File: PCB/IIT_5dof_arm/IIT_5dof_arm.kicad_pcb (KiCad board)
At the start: 2 copper layers, 100 x 100 mm, 59 parts, among them J1 Screw_Terminal_01x02, J2 Conn_01x06, J3 Conn_01x06, J4 Conn_01x06, J5 Conn_01x06, J6 Conn_01x06, J7 Conn_01x06, J9 DE9_Receptacle_MountingHoles, SW1 SW_MAIN, SW15 SW_MOT, U5 XL8574T, U6 MAX3232, U9 4504

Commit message: Eliminate GNDPWR
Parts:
- C10, C11, C12: value 0.1uF -> 10uF
- D5: value SMAJ12A -> SMAJ5.0A
- moved C12 6.08 mm to (136.1, 86.4), turned to 90 degrees
- moved C10 5.80 mm to (127.4, 88.8), turned to -90 degrees
- moved C11 2.62 mm to (64.5, 57.5), turned to 90 degrees
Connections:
- C10 pad 2: GNDPWR -> GND
- C11 pad 2: GNDPWR -> GND
- C12 pad 2: GNDPWR -> GND
- C14 pad 2: GNDPWR -> GND
- D19 pad 2: GNDPWR -> GND
- J1 pad 1: GNDPWR -> GND
- PS1 pad 2: GNDPWR -> GND
- R36 pad 2: GNDPWR -> GND
- SW15 pad 3: GNDPWR -> GND
- U1 pad 4: GNDPWR -> GND
- U2 pad 4: GNDPWR -> GND
- U3 pad 4: GNDPWR -> GND
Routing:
- net GNDPWR: track 204.8 -> 0.00 mm
- net GND: track 2.54 -> 14.0 mm, vias 21 -> 23
- net /mot1_A: track 67.9 -> 69.5 mm
- net /mot1_B: track 65.9 -> 67.2 mm

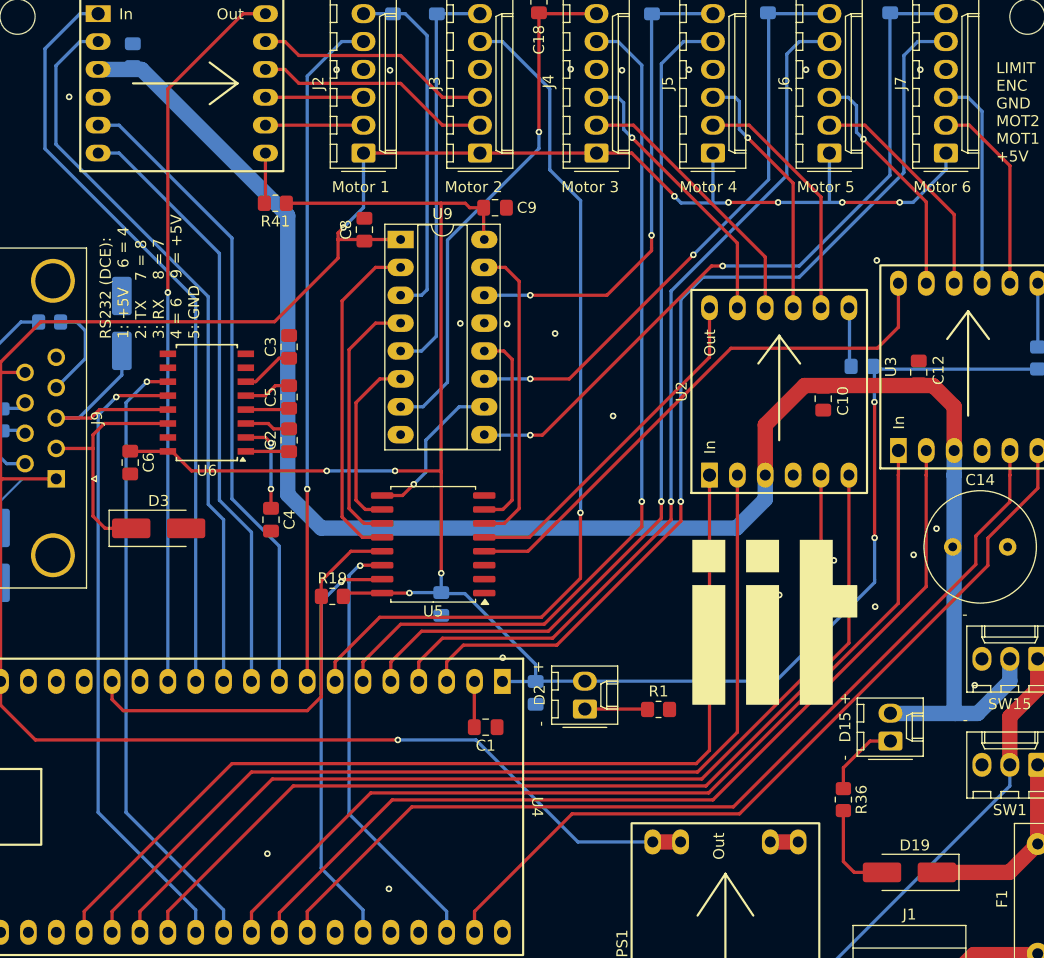
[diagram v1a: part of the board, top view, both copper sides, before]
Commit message: Remove unnecessary vias
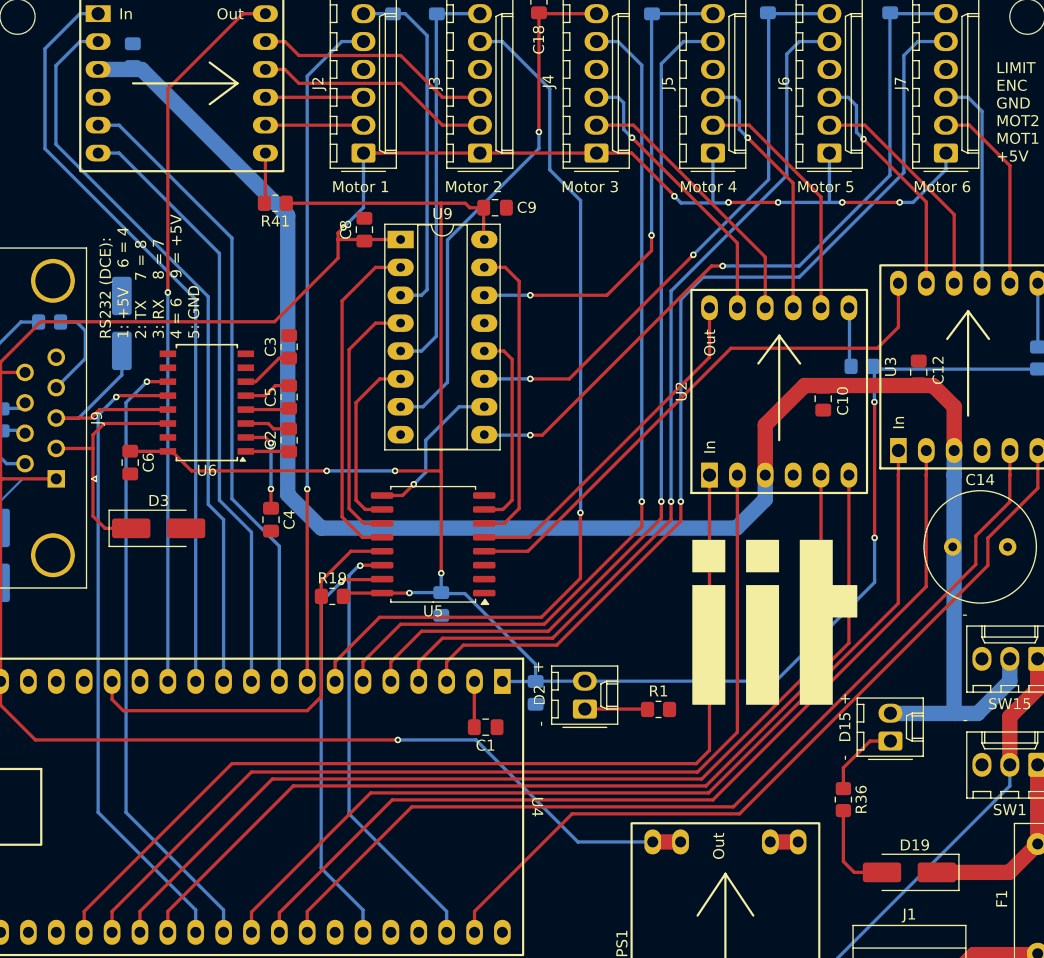
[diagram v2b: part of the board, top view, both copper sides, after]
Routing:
- net GND: vias 23 -> 0
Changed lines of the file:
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@@
 		(tags "capacitor handsolder")
 		(property "Reference" "C12"
-			(at 0.2 1.8 270)
+			(at 0.2 1.8 -90)
 			(layer "F.SilkS")
 			(effects
@@
 		)
 		(property "Value" "10uF"
-			(at 0 1.68 270)
+			(at 0 1.68 -90)
 			(layer "F.Fab")
 			(effects
@@
 		)
 		(fp_text user "${REFERENCE}"
-			(at 0 0 270)
+			(at 0 0 -90)
 			(layer "F.Fab")
 			(effects
@@
 		(tags "capacitor handsolder")
 		(property "Reference" "C11"
-			(at 0.4 1.9 270)
+			(at 0.4 1.9 -90)
 			(layer "B.SilkS")
 			(effects
@@
 		)
 		(property "Value" "10uF"
-			(at 0 -1.68 270)
+			(at 0 -1.68 -90)
 			(layer "B.Fab")
 			(effects
@@
 		)
 		(fp_text user "${REFERENCE}"
-			(at 0 0 270)
+			(at 0 0 -90)
 			(layer "B.Fab")
 			(effects
@@
 		(net 1)
 	)
-	(via
-		(at 125.8316 58.8264)
-		(size 0.6)
-		(drill 0.3)
-		(layers "F.Cu" "B.Cu")
-		(free yes)
-		(net 1)
-	)
-	(via
-		(at 123.3932 106.68)
-		(size 0.6)
-		(drill 0.3)
-		(layers "F.Cu" "B.Cu")
-		(free yes)
-		(net 1)
-	)
-	(via
-		(at 135.636 103.0224)
-		(size 0.6)
-		(drill 0.3)
-		(layers "F.Cu" "B.Cu")
-		(free yes)
-		(net 1)
-	)
-	(via
-		(at 118.11 110.2868)
-		(size 0.6)
-		(drill 0.3)
-		(layers "F.Cu" "B.Cu")
-		(free yes)
-		(net 1)
-	)
-	(via
-		(at 104.394 58.7756)
-		(size 0.6)
-		(drill 0.3)
-		(layers "F.Cu" "B.Cu")
-		(free yes)
-		(net 1)
-	)
-	(via
-		(at 83.058 58.8264)
-		(size 0.6)
-		(drill 0.3)
-		(layers "F.Cu" "B.Cu")
-		(free yes)
-		(net 1)
-	)
-	(via
-		(at 132.1308 107.7468)
-		(size 0.6)
-		(drill 0.3)
-		(layers "F.Cu" "B.Cu")
-		(free yes)
-		(net 1)
-	)
-	(via
-		(at 115.1636 58.8264)
-		(size 0.6)
-		(drill 0.3)
-		(layers "F.Cu" "B.Cu")
-		(free yes)
-		(net 1)
-	)
-	(via
-		(at 98.2 112.4)
-		(size 0.6)
-		(drill 0.3)
-		(layers "F.Cu" "B.Cu")
-		(free yes)
-		(net 1)
-	)
-	(via
-		(at 137.7188 100.6348)
-		(size 0.6)
-		(drill 0.3)
-		(layers "F.Cu" "B.Cu")
-		(free yes)
-		(net 1)
-	)
-	(via
-		(at 98.6028 81.9912)
-		(size 0.6)
-		(drill 0.3)
-		(layers "F.Cu" "B.Cu")
-		(free yes)
-		(net 1)
-	)
-	(via
-		(at 109.0676 58.8772)
-		(size 0.6)
-		(drill 0.3)
-		(layers "F.Cu" "B.Cu")
-		(free yes)
-		(net 1)
-	)
-	(via
-		(at 141.2 114.9)
-		(size 0.6)
-		(drill 0.3)
-		(layers "F.Cu" "B.Cu")
-		(free yes)
-		(net 1)
-	)
-	(via
-		(at 76.7588 130.2512)
-		(size 0.6)
-		(drill 0.3)
-		(layers "F.Cu" "B.Cu")
-		(free yes)
-		(net 1)
-	)
-	(via
-		(at 128.3716 103.5304)
-		(size 0.6)
-		(drill 0.3)
-		(layers "F.Cu" "B.Cu")
-		(free yes)
-		(net 1)
-	)
-	(via
-		(at 108.2548 90.3732)
-		(size 0.6)
-		(drill 0.3)
-		(layers "F.Cu" "B.Cu")
-		(free yes)
-		(net 1)
-	)
-	(via
-		(at 102.9716 82.8548)
-		(size 0.6)
-		(drill 0.3)
-		(layers "F.Cu" "B.Cu")
-		(free yes)
-		(net 1)
-	)
-	(via
-		(at 87.9348 58.8772)
-		(size 0.6)
-		(drill 0.3)
-		(layers "F.Cu" "B.Cu")
-		(free yes)
-		(net 1)
-	)
-	(via
-		(at 132.2832 76.2)
-		(size 0.6)
-		(drill 0.3)
-		(layers "F.Cu" "B.Cu")
-		(free yes)
-		(net 1)
-	)
-	(via
-		(at 136.2456 58.8264)
-		(size 0.6)
-		(drill 0.3)
-		(layers "F.Cu" "B.Cu")
-		(free yes)
-		(net 1)
-	)
-	(via
-		(at 94.3356 81.9404)
-		(size 0.6)
-		(drill 0.3)
-		(layers "F.Cu" "B.Cu")
-		(free yes)
-		(net 1)
-	)
-	(via
-		(at 87.8332 133.4516)
-		(size 0.6)
-		(drill 0.3)
-		(layers "F.Cu" "B.Cu")
-		(free yes)
-		(net 1)
-	)
-	(via
-		(at 58.7 61.3)
-		(size 0.6)
-		(drill 0.3)
-		(layers "F.Cu" "B.Cu")
-		(free yes)
-		(net 1)
-	)

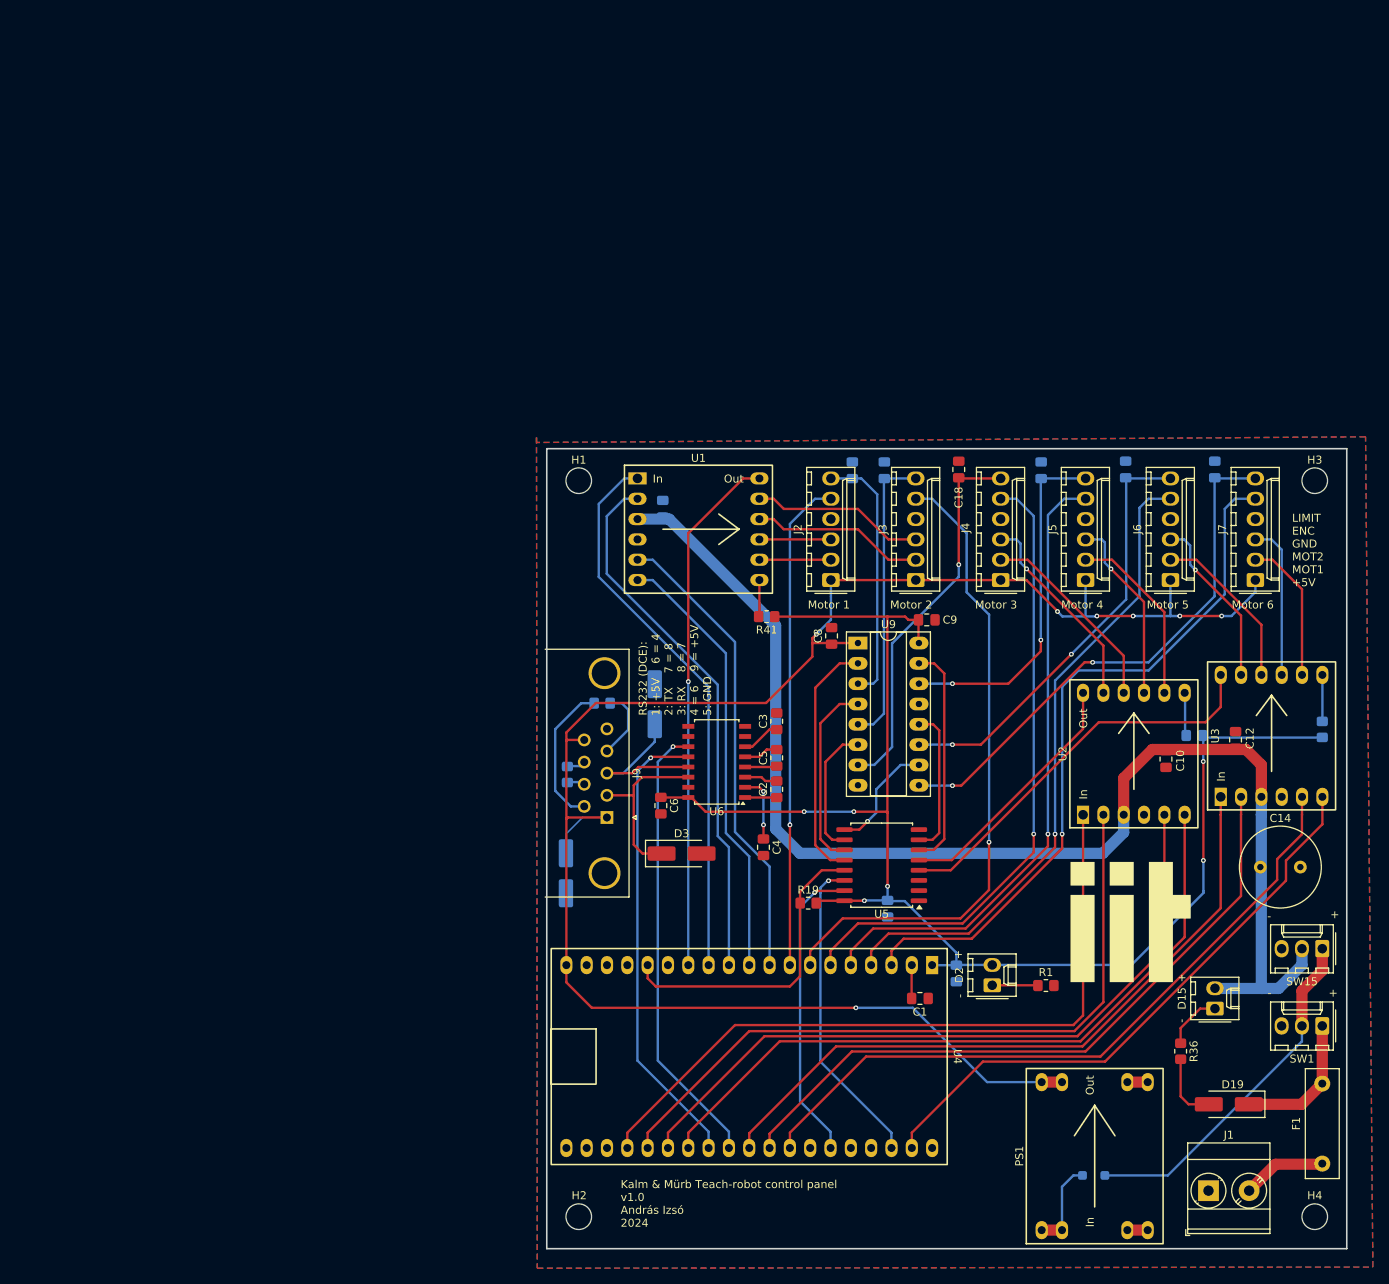
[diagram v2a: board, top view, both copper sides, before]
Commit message: Update schematic with new functionalities
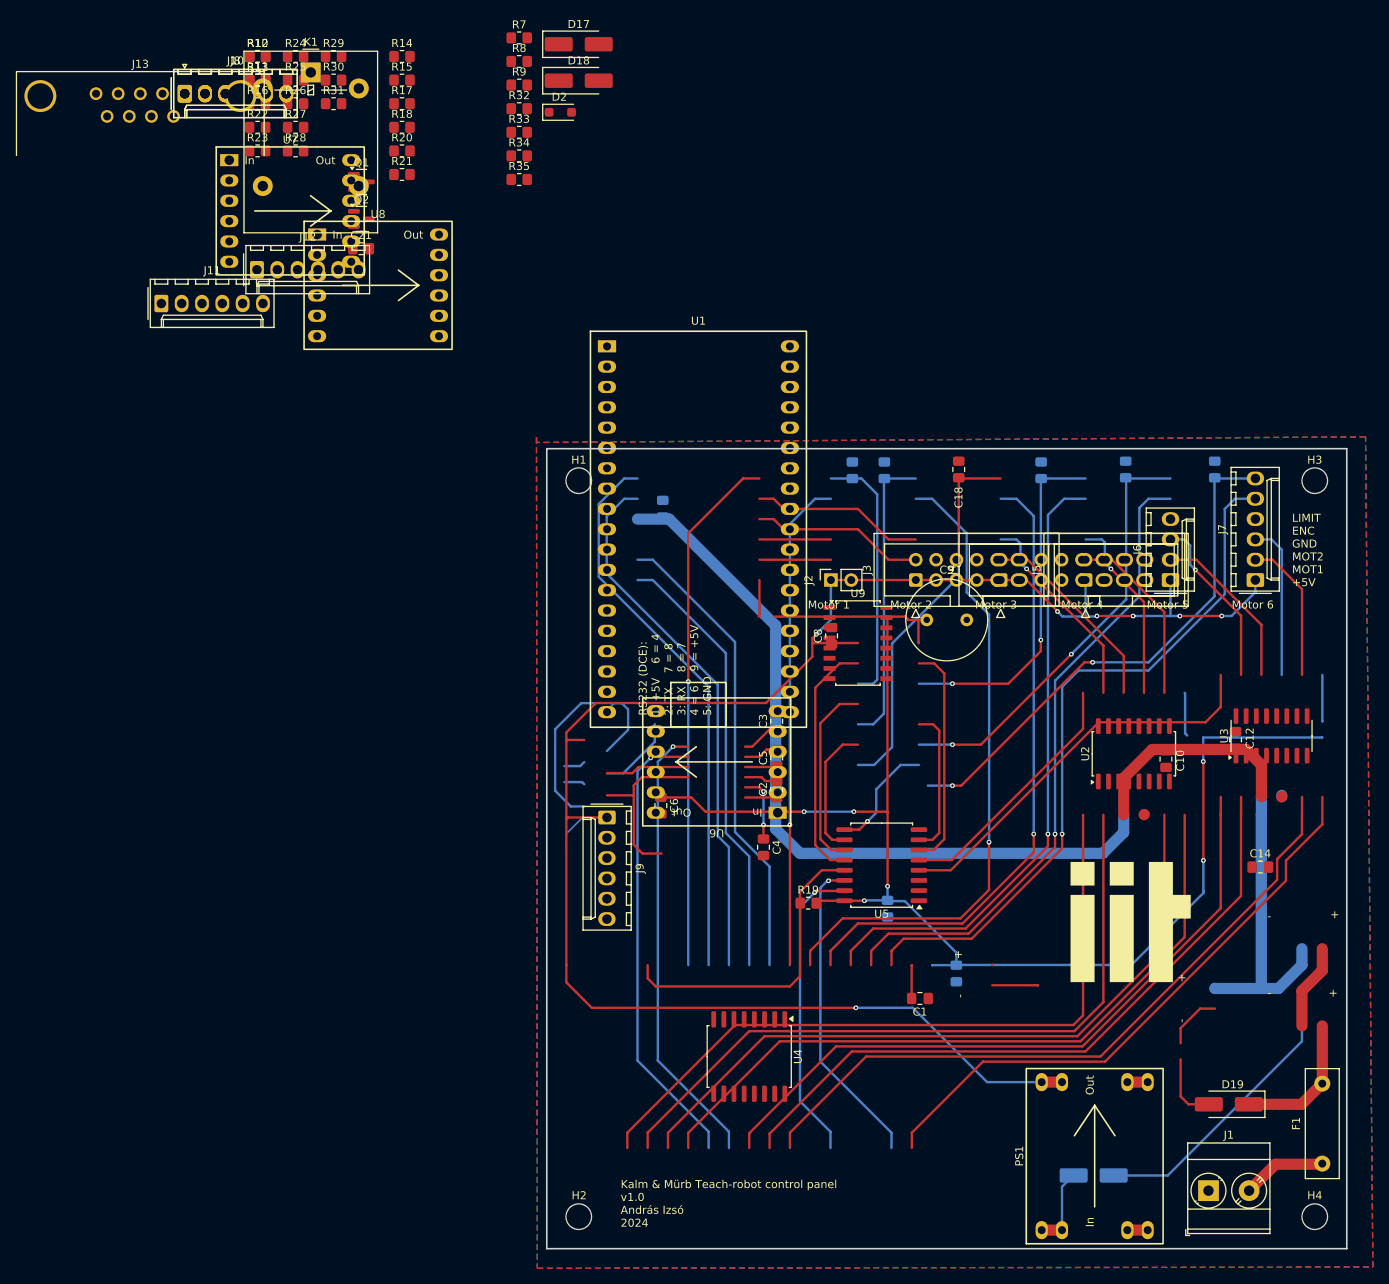
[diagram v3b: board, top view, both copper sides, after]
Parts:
- removed D15: LED, Connector_Molex:Molex_KK-254_AE-6410-02A_1x02_P2.54mm_Vertical
- removed D3, D4: SMAJ12A, Diode_SMD:D_SMA_Handsoldering
- removed D5: SMAJ5.0A, Diode_SMD:D_SMA_Handsoldering
- removed R1: 220, Resistor_SMD:R_0805_2012Metric_Pad1.20x1.40mm_HandSolder
- removed R2, R3: 1k, Resistor_SMD:R_0805_2012Metric_Pad1.20x1.40mm_HandSolder
- removed R36: 590, Resistor_SMD:R_0805_2012Metric_Pad1.20x1.40mm_HandSolder
- removed R41, R42, R43: 10k, Resistor_SMD:R_0805_2012Metric_Pad1.20x1.40mm_HandSolder
- removed SW1: SW_MAIN, Connector_Molex:Molex_KK-254_AE-6410-03A_1x03_P2.54mm_Vertical
- removed SW15: SW_MOT, Connector_Molex:Molex_KK-254_AE-6410-03A_1x03_P2.54mm_Vertical
- added C21: 0.1uF, Capacitor_SMD:C_0805_2012Metric_Pad1.18x1.45mm_HandSolder, F.Cu at (26.8, 25.0)
- added D17: SMAJ12A, Diode_SMD:D_SMA_Handsoldering, F.Cu at (54.0, -0.55)
- added D18: SMAJ12A, Diode_SMD:D_SMA_Handsoldering, F.Cu at (54.0, 4.00)
- added J10, J8: Conn_01x06, Connector_Molex:Molex_KK-254_AE-6410-06A_1x06_P2.54mm_Vertical, F.Cu at (4.74, 5.62)
- added J11: Conn_01x06, Connector_Molex:Molex_KK-254_AE-6410-06A_1x06_P2.54mm_Vertical, F.Cu at (1.82, 31.9)
- added J12: Conn_01x06, Connector_Molex:Molex_KK-254_AE-6410-06A_1x06_P2.54mm_Vertical, F.Cu at (13.8, 27.6)
- added J13: DE9_Receptacle_MountingHoles, Connector_Dsub:DSUB-9_Female_Horizontal_P2.77x2.84mm_EdgePinOffset4.94mm_Housed_MountingHolesOffset7.48mm, F.Cu at (4.74, 5.62)
- added K1: G5LE-1, Relay_THT:Relay_SPDT_Omron-G5LE-1, F.Cu at (20.5, 2.97)
- added Q1: 2N7002, Package_TO_SOT_SMD:SOT-23, F.Cu at (26.8, 16.6)
- added Q2: 2N7002, Package_TO_SOT_SMD:SOT-23, F.Cu at (26.8, 21.3)
- added R10, R12: 1k, Resistor_SMD:R_0805_2012Metric_Pad1.20x1.40mm_HandSolder, F.Cu at (13.9, 0.97)
- added R11: 1k, Resistor_SMD:R_0805_2012Metric_Pad1.20x1.40mm_HandSolder, F.Cu at (13.9, 3.92)
- added R13: 10k, Resistor_SMD:R_0805_2012Metric_Pad1.20x1.40mm_HandSolder, F.Cu at (13.9, 3.92)
- added R14: 10k, Resistor_SMD:R_0805_2012Metric_Pad1.20x1.40mm_HandSolder, F.Cu at (31.9, 0.97)
- added R15: 1k, Resistor_SMD:R_0805_2012Metric_Pad1.20x1.40mm_HandSolder, F.Cu at (31.9, 3.92)
- added R16: 10k, Resistor_SMD:R_0805_2012Metric_Pad1.20x1.40mm_HandSolder, F.Cu at (13.9, 6.88)
- added R17: 1k, Resistor_SMD:R_0805_2012Metric_Pad1.20x1.40mm_HandSolder, F.Cu at (31.9, 6.88)
- added R18: 3k, Resistor_SMD:R_0805_2012Metric_Pad1.20x1.40mm_HandSolder, F.Cu at (31.9, 9.82)
- added R20: 3k, Resistor_SMD:R_0805_2012Metric_Pad1.20x1.40mm_HandSolder, F.Cu at (31.9, 12.8)
- added R21: 3k, Resistor_SMD:R_0805_2012Metric_Pad1.20x1.40mm_HandSolder, F.Cu at (31.9, 15.7)
- added R22: 3k, Resistor_SMD:R_0805_2012Metric_Pad1.20x1.40mm_HandSolder, F.Cu at (13.9, 9.82)
- added R23: 3k, Resistor_SMD:R_0805_2012Metric_Pad1.20x1.40mm_HandSolder, F.Cu at (13.9, 12.8)
- added R24: 10k, Resistor_SMD:R_0805_2012Metric_Pad1.20x1.40mm_HandSolder, F.Cu at (18.6, 0.97)
- added R25: 10k, Resistor_SMD:R_0805_2012Metric_Pad1.20x1.40mm_HandSolder, F.Cu at (18.6, 3.92)
- added R26: 10k, Resistor_SMD:R_0805_2012Metric_Pad1.20x1.40mm_HandSolder, F.Cu at (18.6, 6.88)
- added R27: 10k, Resistor_SMD:R_0805_2012Metric_Pad1.20x1.40mm_HandSolder, F.Cu at (18.6, 9.82)
- added R28: 4k7, Resistor_SMD:R_0805_2012Metric_Pad1.20x1.40mm_HandSolder, F.Cu at (18.6, 12.8)
- added R29: 10k, Resistor_SMD:R_0805_2012Metric_Pad1.20x1.40mm_HandSolder, F.Cu at (23.4, 0.97)
- added R30: 4k7, Resistor_SMD:R_0805_2012Metric_Pad1.20x1.40mm_HandSolder, F.Cu at (23.4, 3.92)
- added R31: 10k, Resistor_SMD:R_0805_2012Metric_Pad1.20x1.40mm_HandSolder, F.Cu at (23.4, 6.88)
- added R32: 1k, Resistor_SMD:R_0805_2012Metric_Pad1.20x1.40mm_HandSolder, F.Cu at (46.6, 7.50)
- added R33: 10k, Resistor_SMD:R_0805_2012Metric_Pad1.20x1.40mm_HandSolder, F.Cu at (46.6, 10.4)
- added R34: 1k, Resistor_SMD:R_0805_2012Metric_Pad1.20x1.40mm_HandSolder, F.Cu at (46.6, 13.4)
- added R35: 2k, Resistor_SMD:R_0805_2012Metric_Pad1.20x1.40mm_HandSolder, F.Cu at (46.6, 16.4)
- added R7: 220, Resistor_SMD:R_0805_2012Metric_Pad1.20x1.40mm_HandSolder, F.Cu at (46.6, -1.35)
- added R8: 100k, Resistor_SMD:R_0805_2012Metric_Pad1.20x1.40mm_HandSolder, F.Cu at (46.6, 1.60)
- added R9: 10k, Resistor_SMD:R_0805_2012Metric_Pad1.20x1.40mm_HandSolder, F.Cu at (46.6, 4.55)
- added U7: ~, IIT_5dof_arm:DRV8833-M, F.Cu at (17.9, 20.3)
- added U8: ~, IIT_5dof_arm:DRV8833-M, F.Cu at (28.9, 29.6)
- C1, C17, C18, C19, C20: value 10nF -> 0.1uF
- C10, C11: value 10uF -> 0.1uF
- C14: value 1000uF -> 0.1uF; footprint Capacitor_THT:C_Radial_D10.0mm_H16.0mm_P5.00mm -> Capacitor_SMD:C_0805_2012Metric_Pad1.18x1.45mm_HandSolder
- C15, C16: value 10nF -> 10uF
- C2, C3, C4, C5, C6, C7, C8: value 0.1uF -> 10nF
- C9: value 0.1uF -> 1000uF; footprint Capacitor_SMD:C_0805_2012Metric_Pad1.18x1.45mm_HandSolder -> Capacitor_THT:C_Radial_D10.0mm_H16.0mm_P5.00mm
- D1: value D_Schottky -> SMAJ12A; footprint Diode_SMD:D_SOD-123F -> Diode_SMD:D_SMA_Handsoldering
- D19: value SMAJ12A -> SMAJ5.0A
- D2: value LED -> D_Schottky; footprint Connector_Molex:Molex_KK-254_AE-6410-02A_1x02_P2.54mm_Vertical -> Diode_SMD:D_SOD-123F
- J2: value Conn_01x06 -> Conn_01x02; footprint Connector_Molex:Molex_KK-254_AE-6410-06A_1x06_P2.54mm_Vertical -> Connector_PinSocket_2.54mm:PinSocket_1x02_P2.54mm_Vertical
- J3: value Conn_01x06 -> Conn_02x06_Odd_Even; footprint Connector_Molex:Molex_KK-254_AE-6410-06A_1x06_P2.54mm_Vertical -> Connector_IDC:IDC-Header_2x06_P2.54mm_Vertical
- J4: value Conn_01x06 -> Conn_02x08_Odd_Even; footprint Connector_Molex:Molex_KK-254_AE-6410-06A_1x06_P2.54mm_Vertical -> Connector_IDC:IDC-Header_2x08_P2.54mm_Vertical
- J5: value Conn_01x06 -> Conn_02x04_Odd_Even; footprint Connector_Molex:Molex_KK-254_AE-6410-06A_1x06_P2.54mm_Vertical -> Connector_IDC:IDC-Header_2x04_P2.54mm_Vertical
- J6: value Conn_01x06 -> Conn_01x04; footprint Connector_Molex:Molex_KK-254_AE-6410-06A_1x06_P2.54mm_Vertical -> Connector_Molex:Molex_KK-254_AE-6410-04A_1x04_P2.54mm_Vertical
- J9: value DE9_Receptacle_MountingHoles -> Conn_01x06; footprint Connector_Dsub:DSUB-9_Female_Horizontal_P2.77x2.84mm_EdgePinOffset4.94mm_Housed_MountingHolesOffset7.48mm -> Connector_Molex:Molex_KK-254_AE-6410-06A_1x06_P2.54mm_Vertical
- R19: value 10k -> 3k
- U1: footprint IIT_5dof_arm:DRV8833-M -> IIT_5dof_arm:NodeMCU32S
- U2: value ~ -> 74LS157; footprint IIT_5dof_arm:DRV8833-M -> Package_SO:SO-16_5.3x10.2mm_P1.27mm
- U3: value ~ -> 4504; footprint IIT_5dof_arm:DRV8833-M -> Package_SO:SOIC-16_3.9x9.9mm_P1.27mm
- U4: value ~ -> XL8574T; footprint IIT_5dof_arm:NodeMCU32S -> Package_SO:SOIC-16W_7.5x10.3mm_P1.27mm
- U6: value MAX3232 -> ~; footprint Package_SO:SOIC-16W_5.3x10.2mm_P1.27mm -> IIT_5dof_arm:DRV8833-M
- U9: value 4504 -> MAX3232; footprint Package_DIP:DIP-16_W7.62mm_Socket_LongPads -> Package_SO:SOIC-16W_5.3x10.2mm_P1.27mm
- moved D2 121.7 mm to (51.7, 7.95), turned to 0 degrees
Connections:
- C1 pad 2: Net-(U4-RESET/EN) -> +3V3
- C10 pad 1: VCC -> +5V
- C11 pad 1: VCC -> +3V3
- C12 pad 1: VCC -> /MotPower
- C14 pad 1: VCC -> +3V3
- C15 pad 1: /Mot4_LIMIT_IN -> /MotPower
- C16 pad 1: /Mot5_LIMIT_IN -> /MotPower
- C17 pad 1: /Mot2_LIMIT_IN -> Net-(U9-C1+)
- C17 pad 2: GND -> Net-(U9-C1-)
- C18 pad 1: /Mot3_LIMIT_IN -> Net-(U9-C2+)
- C18 pad 2: GND -> Net-(U9-C2-)
- C19 pad 1: /Mot6_LIMIT_IN -> +3V3
- C2 pad 1: Net-(U6-C1+) -> GND
- C2 pad 2: Net-(U6-C1-) -> /EspRST
- C20 pad 1: /Mot1_LIMIT_IN -> Net-(U9-VS-)
- C3 pad 1: Net-(U6-VS-) -> /Mot1_LIMIT_IN
- C4 pad 1: Net-(U6-VS+) -> /Mot2_LIMIT_IN
- C5 pad 1: Net-(U6-C2+) -> /Mot3_LIMIT_IN
- C5 pad 2: Net-(U6-C2-) -> GND
- C6 pad 1: +3V3 -> /Mot4_LIMIT_IN
- C7 pad 1: +3V3 -> /Mot5_LIMIT_IN
- C8 pad 1: +5V -> /Mot6_LIMIT_IN
- C9 pad 1: +3V3 -> VCC
- D1 pad 1: Net-(D1-K) -> +15V
- D1 pad 2: Net-(D1-A) -> GND
- D19 pad 1: +15V -> +5V
- D2 pad 2: +3V3 -> /PowerOn
- J2 pad 1: +5V -> /EspRST
- J2 pad 2: /Mot1_OUT1 -> GND
- J3 pad 1: +5V -> +3V3
- J3 pad 2: /Mot2_OUT1 -> /Limit1_LED-
- J3 pad 3: /Mot2_OUT2 -> +3V3
- J3 pad 4: GND -> /Limit2_LED-
- J3 pad 5: /Mot2_ENC -> +3V3
- J3 pad 6: /Mot2_LIMIT_IN -> /Limit3_LED-
- J4 pad 1: +5V -> /PowerOn
- J4 pad 2: /Mot3_OUT1 -> /LED_PowerOn-
- J4 pad 3: /Mot3_OUT2 -> VCC
- J4 pad 4: GND -> /LED_VCC-
- J4 pad 5: /Mot3_ENC -> +3V3
- J4 pad 6: /Mot3_LIMIT_IN -> /LED_3v3-
- J5 pad 1: +5V -> +15V
- J5 pad 2: /Mot4_OUT1 -> /PowerOn
- J5 pad 3: /Mot4_OUT2 -> /PowerOn
- J5 pad 4: GND -> VCC
- J5 pad 5: /Mot4_ENC -> /EMG_signal
- J5 pad 6: /Mot4_LIMIT_IN -> GND
- J6 pad 2: /Mot5_OUT1 -> /ESP-CAM/RX
- J6 pad 3: /Mot5_OUT2 -> /ESP-CAM/TX
- J7 pad 2: /Mot6_OUT1 -> /Mot1_OUT1
- J7 pad 3: /Mot6_OUT2 -> /Mot1_OUT2
- J7 pad 5: /Mot6_ENC -> /Mot1_ENC
- J7 pad 6: /Mot6_LIMIT_IN -> /Mot1_LIMIT_IN
- J9 pad 2: /UI_TX_5v -> /Mot3_OUT1
- J9 pad 3: /UI_RX_5v -> /Mot3_OUT2
- J9 pad 4: Net-(J9-Pad4) -> GND
- J9 pad 5: GND -> /Mot3_ENC
- J9 pad 6: Net-(J9-Pad6) -> /Mot3_LIMIT_IN
- PS1 pad 1: Net-(D1-K) -> Net-(D2-K)
- R19 pad 1: /extender_INT -> /Limit5_LED-
- R19 pad 2: +3V3 -> GND
- U1 pad 1: /mot1_A -> +3V3
- U1 pad 10: /Mot2_OUT1 -> /mot2_A
- U1 pad 11: /Mot2_OUT2 -> /mot2_B
- U1 pad 12: /~{Fault}_12 -> /mot1_B
- U1 pad 2: /mot1_B -> /EspRST
- U1 pad 3: VCC -> /EMG_signal
- U1 pad 4: GND -> /Mot6_ENC
- U1 pad 5: /mot2_A -> /Mot5_ENC
- U1 pad 6: /mot2_B -> /Mot4_ENC
- U1 pad 7: /~{Sleep}_12 -> /Mot3_ENC
- U1 pad 8: /Mot1_OUT1 -> /Mot2_ENC
- U1 pad 9: /Mot1_OUT2 -> /Mot1_ENC/ESP-CAM_RX
- U2 pad 1: /mot4_A -> /useESP-CAM
- U2 pad 10: /Mot3_OUT1 -> /mot1_A/ESP-CAM_TX
- U2 pad 11: /Mot3_OUT2 -> Net-(U2-E)
- U2 pad 12: /~{Fault}_34 -> /alt_mot1_enc
- U2 pad 2: /mot4_B -> /mot1_A/ESP-CAM_TX
- U2 pad 3: VCC -> /alt_mot1A
- U2 pad 4: GND -> /mot1_A
- U2 pad 5: /mot3_A -> /Mot1_ENC
- U2 pad 6: /mot3_B -> /ESP-CAM/RX
- U2 pad 7: /~{Sleep}_34 -> /Mot1_ENC/ESP-CAM_RX
- U2 pad 8: /Mot4_OUT1 -> GND
- U2 pad 9: /Mot4_OUT2 -> /ESP-CAM/TX
- U3 pad 1: /mot5_A -> +5V
- U3 pad 10: /Mot5_OUT1 -> /Mot6_LIMIT
- U3 pad 11: /Mot5_OUT2 -> /Mot5_LIMIT_IN
- U3 pad 12: /~{Fault}_56 -> /Mot5_LIMIT
- U3 pad 2: /mot5_B -> /Mot1_LIMIT
- U3 pad 3: VCC -> /Mot1_LIMIT_IN
- U3 pad 4: GND -> /Mot2_LIMIT
- U3 pad 5: /mot6_A -> /Mot2_LIMIT_IN
- U3 pad 6: /mot6_B -> /Mot3_LIMIT
- U3 pad 7: /~{Sleep}_56 -> /Mot3_LIMIT_IN
- U3 pad 8: /Mot6_OUT1 -> GND
- U3 pad 9: /Mot6_OUT2 -> /Mot6_LIMIT_IN
- U4 pad 1: +3V3 -> Net-(U4-A0)
- U4 pad 10: /mot2_B -> /alt_mot1_enc
- U4 pad 11: /mot1_B -> /TBD_Led1
- U4 pad 12: /mot1_A -> /TBD_Led2
- U4 pad 13: /~{Fault}_12 -> /extender_INT
- U4 pad 14: GND -> /SCL_3v3
- U4 pad 15: /extender_INT -> /SDA_3v3
- U4 pad 16: unconnected-(U4-GPIO9/RX1-Pad16) -> +3V3
- U4 pad 2: Net-(U4-RESET/EN) -> GND
- U4 pad 3: /Mot6_ENC -> GND
- U4 pad 4: /Mot5_ENC -> /~{Fault}_12
- U4 pad 5: /Mot4_ENC -> /Man/Aut SW
- U4 pad 6: /Mot3_ENC -> /MotEnable
- U4 pad 7: /Mot2_ENC -> /useESP-CAM
- U4 pad 8: /Mot1_ENC -> GND
- U4 pad 9: /mot2_A -> /alt_mot1A
- U6 pad 1: Net-(U6-C1+) -> /mot4_A
- U6 pad 10: unconnected-(U6-T2IN-Pad10) -> /Mot3_OUT1
- U6 pad 11: /UI_TX_3v3 -> /Mot3_OUT2
- U6 pad 12: /UI_RX_3v3 -> /~{Fault}_34
- U6 pad 2: Net-(U6-VS+) -> /mot4_B
- U6 pad 3: Net-(U6-C1-) -> /MotPower
- U6 pad 4: Net-(U6-C2+) -> GND
- U6 pad 5: Net-(U6-C2-) -> /mot3_A
- U6 pad 6: Net-(U6-VS-) -> /mot3_B
- U6 pad 7: unconnected-(U6-T2OUT-Pad7) -> /~{Sleep}_34
- U6 pad 8: unconnected-(U6-R2IN-Pad8) -> /Mot4_OUT1
- U6 pad 9: unconnected-(U6-R2OUT-Pad9) -> /Mot4_OUT2
- U9 pad 1: +5V -> Net-(U9-C1+)
- U9 pad 10: /Mot6_LIMIT -> unconnected-(U9-T2IN-Pad10)
- U9 pad 11: /Mot5_LIMIT_IN -> /UI_TX_3v3
- U9 pad 12: /Mot5_LIMIT -> /UI_RX_3v3
- U9 pad 13: GND -> /UI_RX_5v
- U9 pad 14: /Mot4_LIMIT_IN -> /UI_TX_5v
- U9 pad 15: /Mot4_LIMIT -> GND
- U9 pad 2: /Mot1_LIMIT -> Net-(U9-VS+)
- U9 pad 3: /Mot1_LIMIT_IN -> Net-(U9-C1-)
- U9 pad 4: /Mot2_LIMIT -> Net-(U9-C2+)
- U9 pad 5: /Mot2_LIMIT_IN -> Net-(U9-C2-)
- U9 pad 6: /Mot3_LIMIT -> Net-(U9-VS-)
- U9 pad 7: /Mot3_LIMIT_IN -> unconnected-(U9-T2OUT-Pad7)
- U9 pad 8: GND -> unconnected-(U9-R2IN-Pad8)
- U9 pad 9: /Mot6_LIMIT_IN -> unconnected-(U9-R2OUT-Pad9)
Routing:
- net +3V3: track 180.3 -> 270.8 mm
- net /mot3_A: track 90.3 -> 0.00 mm
- net /alt_mot1A: track 0.00 -> 90.3 mm
- net /Mot6_ENC: track 88.8 -> 0.00 mm, vias 1 -> 0
- net /Mot1_ENC: track 61.6 -> 150.3 mm, vias 1 -> 2
- net /mot5_A: track 86.3 -> 0.00 mm
- net (no net): track 0.00 -> 62.8 mm
- net Net-(D1-A): track 44.2 -> 0.00 mm
- net Net-(U9-C1+): track 0.00 -> 37.1 mm
- net GND: track 14.0 -> 47.5 mm
- net Net-(U9-VS-): track 0.00 -> 32.4 mm
- net /Mot1_LIMIT_IN: track 32.4 -> 0.00 mm
- net /Mot2_LIMIT_IN: track 37.1 -> 8.45 mm, vias 0 -> 2
- net /mot5_B: track 85.4 -> 107.1 mm
- net /Mot2_OUT2: track 21.7 -> 0.00 mm
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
